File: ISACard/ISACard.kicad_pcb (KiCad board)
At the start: 2 copper layers, 171.5 x 95.9 mm, 98 parts, among them J1 Bus_ISA_8bit, J2 ICSP, J3 EXTSPI, J4 SERCON, J5 Conn_01x16, Q1 2N3904, SW1 SW_Push, U1 74LS86, U10 28C256, U11 ATmega328P-P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

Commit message: Fixed some problems with the card...
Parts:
- removed JP16: A7, Connector_PinHeader_2.54mm:PinHeader_1x02_P2.54mm_Vertical
- removed R16: 10k, Resistor_THT:R_Axial_DIN0207_L6.3mm_D2.5mm_P7.62mm_Horizontal
- moved JP18 4.80 mm to (145.3, 89.4)
- moved C13 3.14 mm to (145.2, 100.9)
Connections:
- J1 pad 42: unconnected-(J1-Pad42) -> AEN
- JP15 pad 2: Net-(JP15-Pad2) -> Net-(JP15-B)
- JP17 pad 2: Net-(JP17-Pad2) -> Net-(JP17-C)
- R15 pad 2: Net-(JP15-Pad2) -> Net-(JP15-B)
- U3 pad 11: SEL8255 -> Net-(U3-Pad11)
- U4 pad 11: unconnected-(U4-Pad11) -> SEL8255
- U4 pad 12: GND -> Net-(U3-Pad11)
- U4 pad 13: GND -> AEN
- U7 pad 1: A12 -> A13
- U7 pad 2: Net-(JP16-Pad2) -> Net-(JP15-B)
- U7 pad 4: A13 -> GND
- U7 pad 5: Net-(JP15-Pad2) -> GND
- U7 pad 6: Net-(U7-Pad6) -> unconnected-(U7-Pad6)
- U8 pad 11: unconnected-(U8-Pad11) -> Net-(U8-Pad11)
- U8 pad 12: GND -> Net-(U8-Pad12)
- U8 pad 13: GND -> AEN
- U8 pad 8: Net-(U8-Pad8) -> Net-(U8-Pad12)
- U9 pad 10: Net-(JP17-Pad2) -> GND
- U9 pad 12: Net-(U8-Pad8) -> Net-(U8-Pad11)
- U9 pad 2: Net-(U7-Pad6) -> Net-(U7-Pad11)
- U9 pad 4: Net-(U7-Pad11) -> Net-(JP17-C)
- U9 pad 6: Net-(U9-Pad6) -> Net-(U9-Pad13)
- U9 pad 8: Net-(U9-Pad13) -> unconnected-(U9-Pad8)
- U9 pad 9: Net-(U9-Pad6) -> GND
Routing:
- net AEN: track 0.00 -> 179.1 mm, vias 0 -> 4
- net Net-(JP15-Pad2): track 46.5 -> 0.00 mm, vias 1 -> 0
- net Net-(JP16-Pad2): track 40.9 -> 0.00 mm, vias 1 -> 0
- net Net-(U8-Pad8): track 38.1 -> 0.00 mm, vias 1 -> 0
- net Net-(JP15-B): track 0.00 -> 35.4 mm
- net Net-(U8-Pad11): track 0.00 -> 32.6 mm, vias 0 -> 1
- net Net-(U3-Pad11): track 0.00 -> 29.9 mm, vias 0 -> 1
- net SEL8255: track 113.5 -> 87.4 mm
- net Net-(U7-Pad6): track 18.7 -> 0.00 mm
- net Net-(JP17-C): track 0.00 -> 14.0 mm
- net Net-(U8-Pad12): track 0.00 -> 12.0 mm
- net RESET: track 203.2 -> 211.1 mm
- net Net-(U9-Pad6): track 7.62 -> 0.00 mm
- net GND: track 42.0 -> 47.6 mm, vias 3 -> 4
- net Net-(JP17-Pad2): track 5.34 -> 0.00 mm
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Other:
- board text removed: "M12"

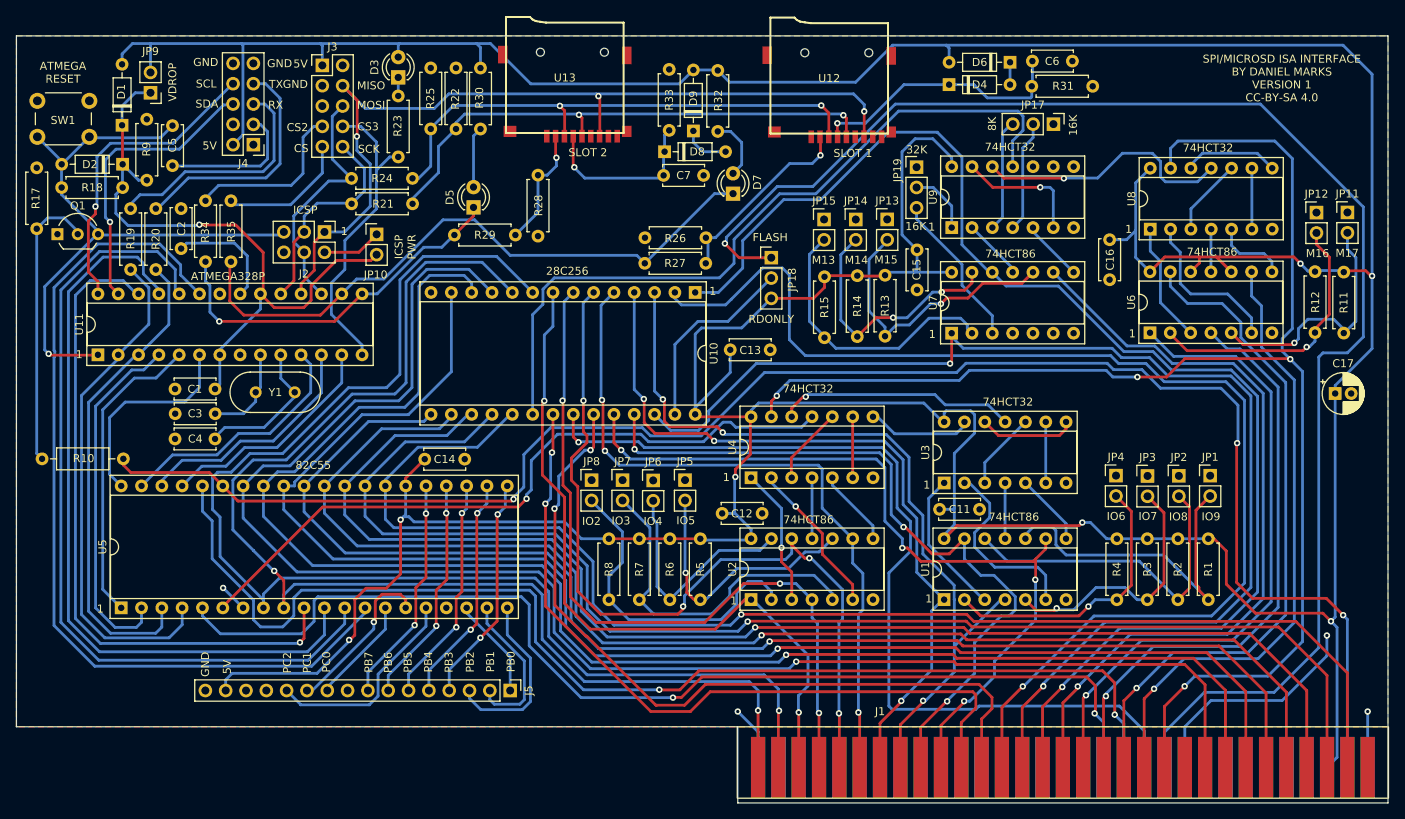
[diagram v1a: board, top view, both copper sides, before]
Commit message: Rearranged the order of the logic
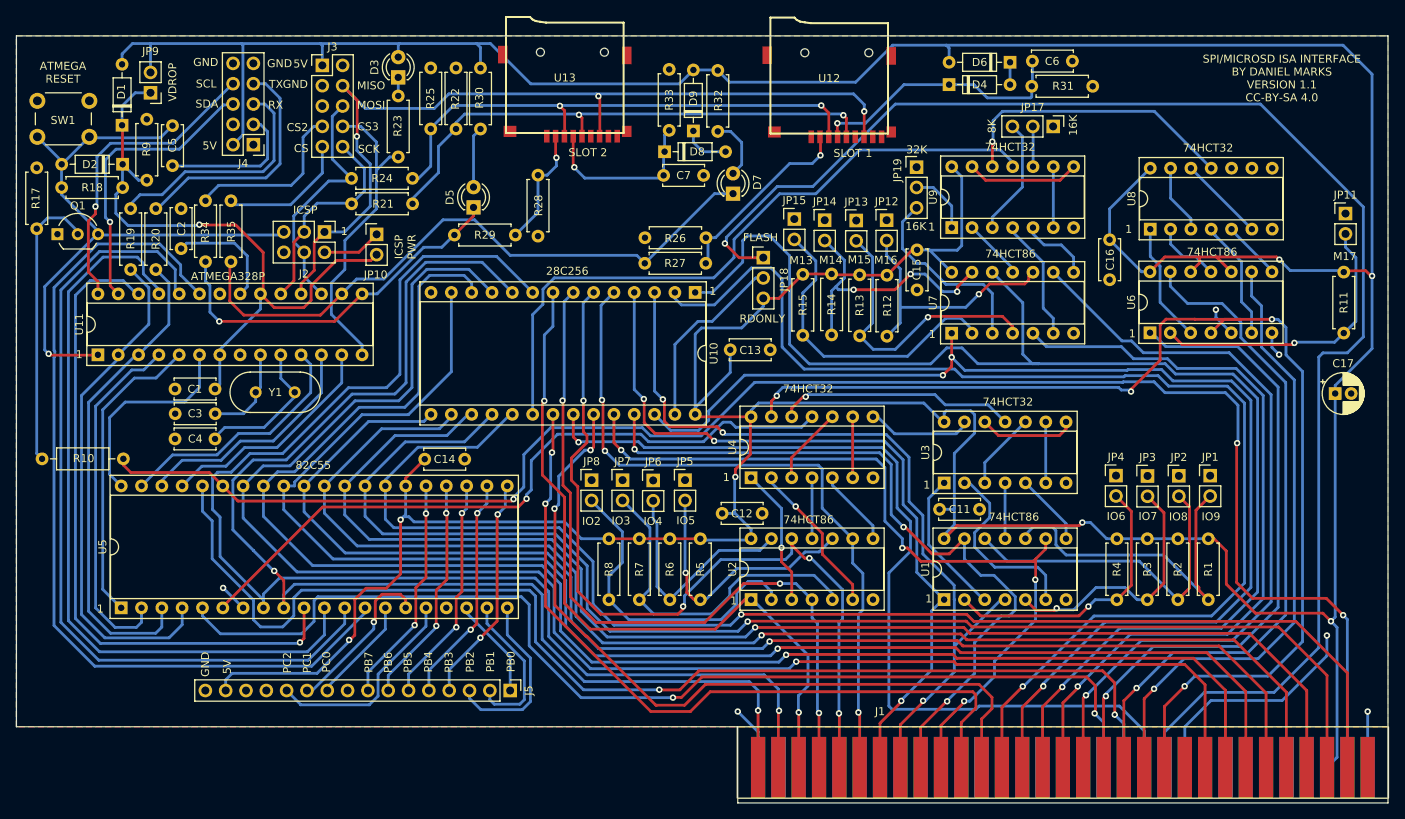
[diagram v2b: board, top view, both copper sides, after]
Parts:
- moved JP12 53.7 mm to (159.8, 84.7)
- moved R12 53.5 mm to (159.8, 91.5)
- moved JP14 3.88 mm to (152.0, 84.7)
- moved JP13 3.87 mm to (156.0, 84.7)
- moved JP15 3.72 mm to (148.2, 84.5)
- moved R14 3.22 mm to (152.9, 91.4)
- moved R13 3.17 mm to (156.4, 91.5)
- moved R15 2.73 mm to (149.3, 91.4)
- moved JP18 1.00 mm to (144.3, 89.3)
- moved JP17 0.29 mm to (180.6, 73.0)
- moved JP11 0.28 mm to (217.1, 83.8)
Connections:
- U6 pad 1: A16 -> A17
- U6 pad 2: Net-(JP12-B) -> Net-(JP11-B)
- U6 pad 4: A17 -> AEN
- U6 pad 5: Net-(JP11-B) -> GND
- U7 pad 10: Net-(JP13-B) -> Net-(JP12-B)
- U7 pad 4: GND -> Net-(JP13-B)
- U7 pad 5: GND -> A15
- U7 pad 6: unconnected-(U7-Pad6) -> Net-(U7-Pad6)
- U7 pad 9: A15 -> A16
- U8 pad 10: Net-(U8-Pad10) -> GND
- U8 pad 13: AEN -> Net-(U8-Pad13)
- U8 pad 2: Net-(U6-Pad6) -> Net-(U6-Pad11)
- U8 pad 3: Net-(U8-Pad10) -> Net-(U8-Pad13)
- U8 pad 4: Net-(U6-Pad11) -> Net-(U6-Pad6)
- U8 pad 6: Net-(U8-Pad6) -> Net-(U8-Pad12)
- U8 pad 8: Net-(U8-Pad12) -> unconnected-(U8-Pad8)
- U8 pad 9: Net-(U8-Pad6) -> GND
- U9 pad 10: GND -> Net-(JP17-C)
- U9 pad 4: Net-(JP17-C) -> Net-(U7-Pad6)
- U9 pad 6: Net-(U9-Pad13) -> Net-(U9-Pad6)
- U9 pad 8: unconnected-(U9-Pad8) -> Net-(U9-Pad13)
- U9 pad 9: GND -> Net-(U9-Pad6)
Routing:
- net AEN: track 179.1 -> 147.0 mm
- net Net-(U7-Pad6): track 0.00 -> 15.3 mm
- net A16: track 81.6 -> 96.6 mm
- net Net-(U8-Pad10): track 9.72 -> 0.00 mm
- net SELROM: track 94.3 -> 84.6 mm
- net Net-(JP17-C): track 14.0 -> 5.05 mm
- net Net-(U8-Pad13): track 0.00 -> 8.67 mm
- net +5V: track 639.9 -> 631.5 mm
- net Net-(U9-Pad6): track 0.00 -> 7.62 mm
- net Net-(U8-Pad6): track 7.62 -> 0.00 mm
- net A17: track 74.1 -> 81.7 mm
- net GND: track 47.6 -> 54.4 mm, vias 4 -> 6
- net Net-(JP11-B): track 31.4 -> 36.5 mm
- net Net-(U6-Pad6): track 19.9 -> 15.0 mm
- net Net-(JP19-B): track 19.6 -> 24.4 mm
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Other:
- board text added: "SPI/MICROSD ISA INTERFACE BY DANIEL MARKS VERSION 1.1 CC-BY-SA 4.0"
- board text removed: "SPI/MICROSD ISA INTERFACE BY DANIEL MARKS VERSION 1 CC-BY-SA 4.0"

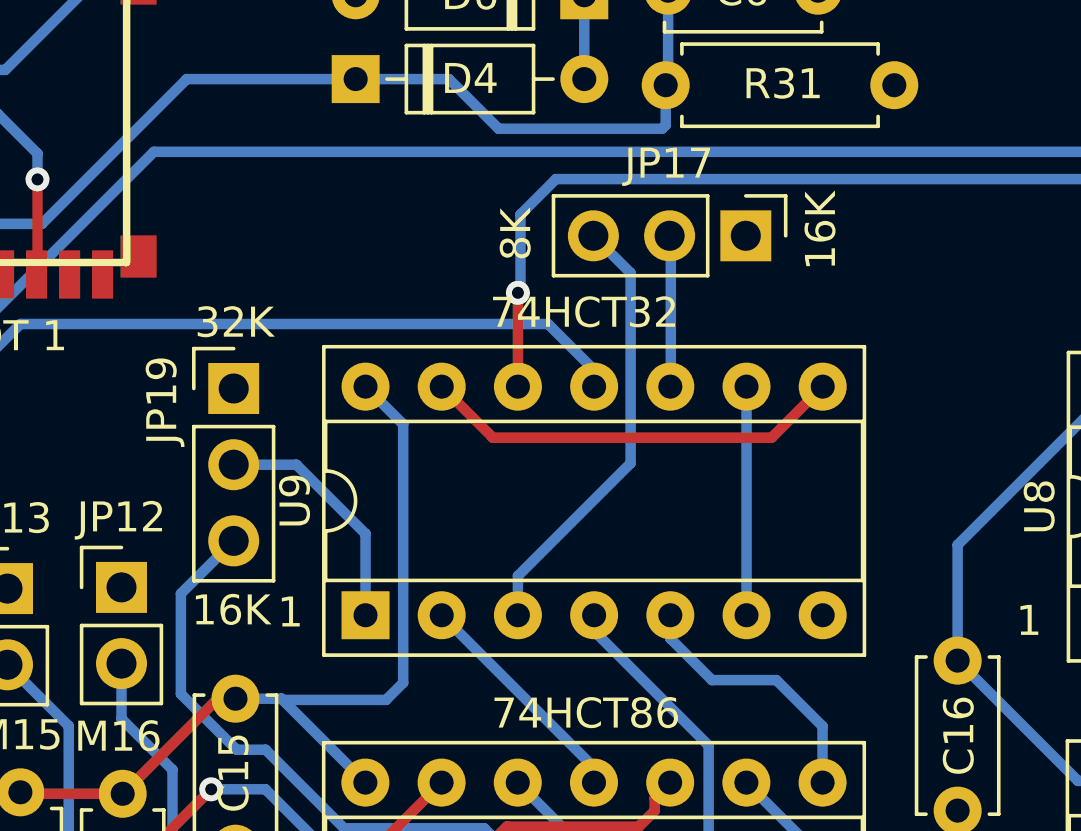
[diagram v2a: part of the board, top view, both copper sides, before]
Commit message: fixed rom labels
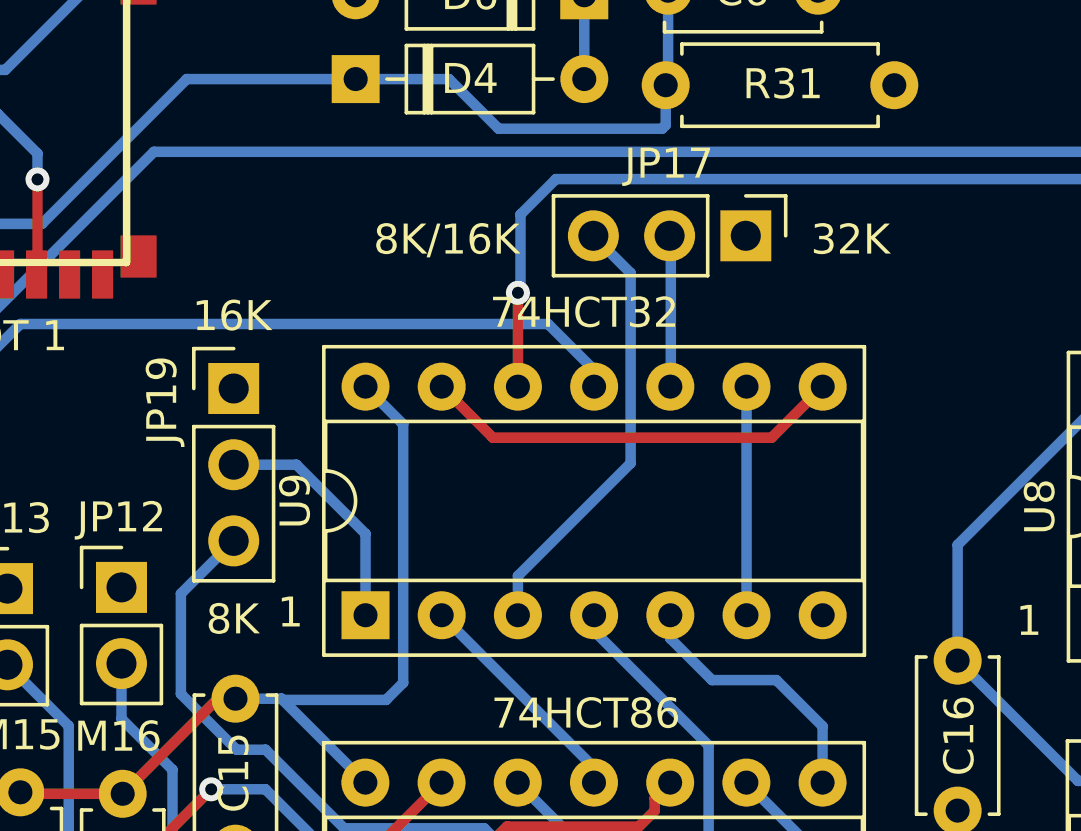
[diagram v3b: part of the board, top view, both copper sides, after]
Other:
- board text added: "8K/16K"
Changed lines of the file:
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@@
     (effects (font (size 1 1) (thickness 0.15)))
   )
-  (gr_text "32K" (at 163.52 75.85) (layer "F.SilkS")
+  (gr_text "32K" (at 184.058 73.08) (layer "F.SilkS")
     (effects (font (size 1 1) (thickness 0.15)))
   )
@@
     (effects (font (size 1 1) (thickness 0.15)))
   )
-  (gr_text "16K" (at 163.41 85.44) (layer "F.SilkS")
+  (gr_text "8K/16K" (at 170.596 73.08) (layer "F.SilkS")
     (effects (font (size 1 1) (thickness 0.15)))
   )
@@
     (effects (font (size 1 1) (thickness 0.15)))
   )
-  (gr_text "16K" (at 183.08 72.79 90) (layer "F.SilkS")
+  (gr_text "16K" (at 163.44 75.63) (layer "F.SilkS")
     (effects (font (size 1 1) (thickness 0.15)))
   )
@@
     (effects (font (size 1 1) (thickness 0.15)))
   )
-  (gr_text "8K" (at 172.92 72.91 90) (layer "F.SilkS")
+  (gr_text "8K" (at 163.46 85.74) (layer "F.SilkS")
     (effects (font (size 1 1) (thickness 0.15)))
   )
